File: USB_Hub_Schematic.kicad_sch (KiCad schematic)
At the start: 0 parts

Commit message: Started KiCAD
Put all relevant ports/chips into KiCAD
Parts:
- added Card1: TF PUSH, lcsc_easyeda:TF-SMD_TF-PUSH, symbol lcsc_easyeda:TFPUSH
- added U1: CH339W_C25503971, lcsc_easyeda:QFN-68_L8.0-W8.0-P0.40-BL-EP5.5, symbol lcsc_easyeda:CH339W_C25503971
- added USB1, USB2: TYPE-C 16PIN 2MD, lcsc_easyeda:USB-C-SMD_TYPE-C-16PIN-2MD-073, symbol lcsc_easyeda:TYPE-C16PIN2MD
- added USB3, USB4: 10.0 QHHTZB6.3, lcsc_easyeda:USB-A-TH_10.0QHHTZB6.3, symbol lcsc_easyeda:10.0QHHTZB6.3

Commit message: New parts
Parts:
- removed U1: CH339W_C25503971, lcsc_easyeda:QFN-68_L8.0-W8.0-P0.40-BL-EP5.5, symbol lcsc_easyeda:CH339W_C25503971
- removed USB1, USB2: TYPE-C 16PIN 2MD, lcsc_easyeda:USB-C-SMD_TYPE-C-16PIN-2MD-073, symbol lcsc_easyeda:TYPE-C16PIN2MD
- removed USB3, USB4: 10.0 QHHTZB6.3, lcsc_easyeda:USB-A-TH_10.0QHHTZB6.3, symbol lcsc_easyeda:10.0QHHTZB6.3
- added U1: Microchip, lcsc_easyeda:VQFN-100_L12.0-W12.0-P0.40-TL-EP8.0, symbol lcsc_easyeda:USB5807C_KD
- added U2: USB-C Male, lcsc_easyeda:USB-C-SMD_TYPE-C-24P-GTJB-040, symbol lcsc_easyeda:TYPE-C24P-GTJB040
- added U3: USB-A Male, lcsc_easyeda:USB-3.0-A-SMD_HC-USB3.0-C26, symbol lcsc_easyeda:HC-USB3.0-C26
- added U4, U5: Multiplexer, lcsc_easyeda:DHVQFN-20_L4.5-W2.5-P0.50-BL-EP, symbol lcsc_easyeda:HD3SS3212IRKSR
- added U6: SD Reader, lcsc_easyeda:HQFN-32_L5.0-W5.0-P0.50-BL-EP3.0, symbol lcsc_easyeda:GL3224-OIY04
- added USB1, USB2: USB-C Female, lcsc_easyeda:TYPE-C-SMD_C9900025773, symbol lcsc_easyeda:TYPE-C24PQT143
- added USB3, USB4: USB-A Female, lcsc_easyeda:USB-A-SMD_U-A-39SS-W-1, symbol lcsc_easyeda:U-A-39SS-W-1
- renumbered Card1 to microSD
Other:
- moved on the sheet: microSD

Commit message: KiCAD Work
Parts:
- removed U1: Microchip, lcsc_easyeda:VQFN-100_L12.0-W12.0-P0.40-TL-EP8.0, symbol lcsc_easyeda:USB5807C_KD
- added C1, C2, C3, C4, C6, C7, C8, C9: 0.1 uF, symbol Device:C
- added R1: 12k, symbol Device:R
- added R2: 900k, symbol Device:R
- added U1, U8: TUSB321, lcsc_easyeda:X2QFN-12_L1.6-W1.6-P0.40-BL, symbol lcsc_easyeda:TUSB321AIRWBR
- added U7: USB5926C-I/KD, lcsc_easyeda:VQFN-100_L12.0-W12.0-P0.40-TL-EP8.1, symbol lcsc_easyeda:USB5926C-I_KD
- added X1: 25MHz, lcsc_easyeda:OSC-SMD_4P-L3.2-W2.5-BL, symbol lcsc_easyeda:CO32H4-25.000-33JDTSN
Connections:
- net GNDREF: now reaches USB3.10 (GND)
- net GNDREF: now also USB1.15 (EP), USB1.16 (EP), USB1.17 (EP), USB1.18 (EP), USB1.A1 (GND), USB1.A12 (GND), USB1.B1 (GND), USB1.B12 (GND), USB3.11 (GND), USB3.4 (GND), USB3.7 (GND), USB4.10 (GND), USB4.11 (GND), USB4.4 (GND), USB4.7 (GND), R1.1, U1.10 (GND), U7.101 (EP), U7.23 (TESTEN)
- net at USB3.2 (D-): now also U7.87 (USB2DN_DM4/PRT_DIS_M4)
- net at USB3.3 (D+): now also U7.86 (USB2DN_DP4/PRT_DIS_P4)
- net at USB3.5 (SSRX-): now also U7.92 (USB3DN_RXDM4)
- net at USB3.6 (SSRX+): now also U7.91 (USB3DN_RXDP4)
- net at USB3.8 (SSTX-): now also C1.2
- net at USB3.9 (SSTX+): now also C2.2
- net at USB4.2 (D-): now also U7.44 (USB2DN_DM3/PRT_DIS_M3)
- net at USB4.3 (D+): now also U7.43 (USB2DN_DP3/PRT_DIS_P3)
- net at USB4.5 (SSRX-): now also U7.49 (USB3DN_RXDM3)
- net at USB4.6 (SSRX+): now also U7.48 (USB3DN_RXDP3)
- net at USB4.8 (SSTX-): now also C3.2
- net at USB4.9 (SSTX+): now also C4.2
- net at USB1.A10 (SSRXn2): now also U7.34 (USB3DN_RXDM2A)
- net at USB1.A11 (SSRXp2): now also U7.33 (USB3DN_RXDP2A)
- net at USB1.A2 (SSTXP1): now also C7.2
- net at USB1.A3 (SSTXn1): now also C6.2
- net at USB1.A4 (VBUS): now also USB1.A9 (VBUS)
- net at USB1.A5 (CC1): now also U1.1 (CC1)
- net at USB1.A6 (DP1): now also USB1.B6 (DP2), U7.35 (USB2DN_DP6/PRT_DIS_P6)
- net at USB1.A7 (DN1): now also USB1.B7 (DN2), U7.36 (USB2DN_DM6/PRT_DIS_M6)
- net at USB1.B10 (SSRXn1): now also U7.41 (USB3DN_RXDM2B)
- net at USB1.B11 (SSRXp1): now also U7.40 (USB3DN_RXDP2B)
- net at USB1.B2 (SSTXp2): now also C9.2
- net at USB1.B3 (SSTXn2): now also C8.2
- net at USB1.B4 (VBUS): now also USB1.B9 (VBUS)
- net at USB1.B5 (CC2): now also U1.2 (CC2)
- new net: R1.2, U7.1 (RBIAS)
- new net: U7.10 (VDD12), U7.17 (VDD12), U7.26 (VDD12), U7.32 (VDD12), U7.39 (VDD12), U7.47 (VDD12)
- new net: U7.2 (VDD33), U7.27 (VDD33), U7.42 (VDD33), U7.5 (VDD33)
- new net: C7.1, U7.30 (USB3DN_TXDP2A)
- new net: C6.1, U7.31 (USB3DN_TXDM2A)
- new net: C9.1, U7.37 (USB3DN_TXDP2B)
- new net: C8.1, U7.38 (USB3DN_TXDM2B)
- new net: C4.1, U7.45 (USB3DN_TXDP3)
- new net: C3.1, U7.46 (USB3DN_TXDM3)
- new net: U7.54 (VDD33), U7.64 (VDD33), U7.72 (VDD33), U7.93 (VDD33)
- new net: U7.59 (VDD12), U7.78 (VDD12), U7.83 (VDD12), U7.90 (VDD12), U7.98 (VDD12)
- new net: C2.1, U7.88 (USB3DN_TXDP4)
- new net: C1.1, U7.89 (USB3DN_TXDM4)
- new net: U1.12 (VDD), U1.4 (PORT)
- new net: R2.1, U1.5 (VBUS_DET)
- no-connect marks 0 -> 7
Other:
- note added: "1.2V PWR"
- note added: "3.3V PWR"
- note added: "CONNECT VBUS TO 5V POWER"
- moved on the sheet: microSD

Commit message: Continued schematics
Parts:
- removed U5: Multiplexer, lcsc_easyeda:DHVQFN-20_L4.5-W2.5-P0.50-BL-EP, symbol lcsc_easyeda:HD3SS3212IRKSR
- removed microSD: TF PUSH, lcsc_easyeda:TF-SMD_TF-PUSH, symbol lcsc_easyeda:TFPUSH
- added Card1: SD Reader, lcsc_easyeda:TF-SMD_TF-PUSH, symbol lcsc_easyeda:TFPUSH
- added D1: LED, symbol Device:LED
- added R3: 4.7k, symbol Device:R
- added R4: 680, 1%, symbol Device:R
- added R5: 330, symbol Device:R
- added X2: 25MHz, lcsc_easyeda:OSC-SMD_4P-L3.2-W2.5-BL, symbol lcsc_easyeda:CO32H4-25.000-33JDTSN
- C2: value 0.1 uF -> 1uF
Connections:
- net GNDREF: now also C2.1, C2.2, U6.24 (VUHSI), U6.27 (GND), U6.28 (SD_WP), U6.33 (EP), R4.2
- net at U7.6 (USB2DN_DP1/PRT_DIS_P1): now also USB3.3 (D+)
- net at U7.7 (USB2DN_DM1/PRT_DIS_M1): now also USB3.2 (D-)
- net at U7.86 (USB2DN_DP4/PRT_DIS_P4): now also U6.32 (DP); no longer USB3.3 (D+)
- net at U7.87 (USB2DN_DM4/PRT_DIS_M4): now also U6.31 (DM); no longer USB3.2 (D-)
- net at U7.88 (USB3DN_TXDP4): now also U6.2 (TXP); no longer C2.1
- net at U7.89 (USB3DN_TXDM4): now also U6.1 (TXN); no longer C1.1
- net at U7.91 (USB3DN_RXDP4): now also U6.5 (RXP); no longer USB3.6 (SSRX+)
- net at U7.92 (USB3DN_RXDM4): now also U6.4 (RXN); no longer USB3.5 (SSRX-)
- net at U1.12 (VDD): now also R2.2, R3.1; no longer U1.4 (PORT)
- net at USB3.8 (SSTX-): no longer C1.2
- net at USB3.9 (SSTX+): no longer C2.2
- net at U6.14 (LED): now also D1.1 (K)
- net at U6.18 (SD_D1): now also Card1.8 (DAT1)
- net at U6.19 (SD_D0): now also Card1.7 (DAT0)
- net at U6.20 (SD_CK): now also Card1.5 (CLX)
- net at U6.21 (SD_CM): now also Card1.3 (CMD)
- net at U6.22 (SD_D3): now also Card1.2 (CD/DAT3)
- net at U6.23 (SD_D2): now also Card1.1 (DAT2)
- net at U6.26 (SD_VCC): now also C1.2, Card1.4 (VDD)
- net at U6.29 (SD_CDZ): now also Card1.CD
- net at U6.9 (RTERM): now also R4.1
- net at USB1.A4 (VBUS), USB1.A9 (VBUS): now also USB1.B4 (VBUS), USB1.B9 (VBUS)
- new net: R3.2, U1.4 (PORT)
- new net: D1.2 (A), R5.2
- new net: C1.1, Card1.10, Card1.11, Card1.12, Card1.13, Card1.6 (VSS)
- no-connect marks 7 -> 18
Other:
- note added: "TO 3.3V PWR"
- note added: "VBUS TO 5V POWER"

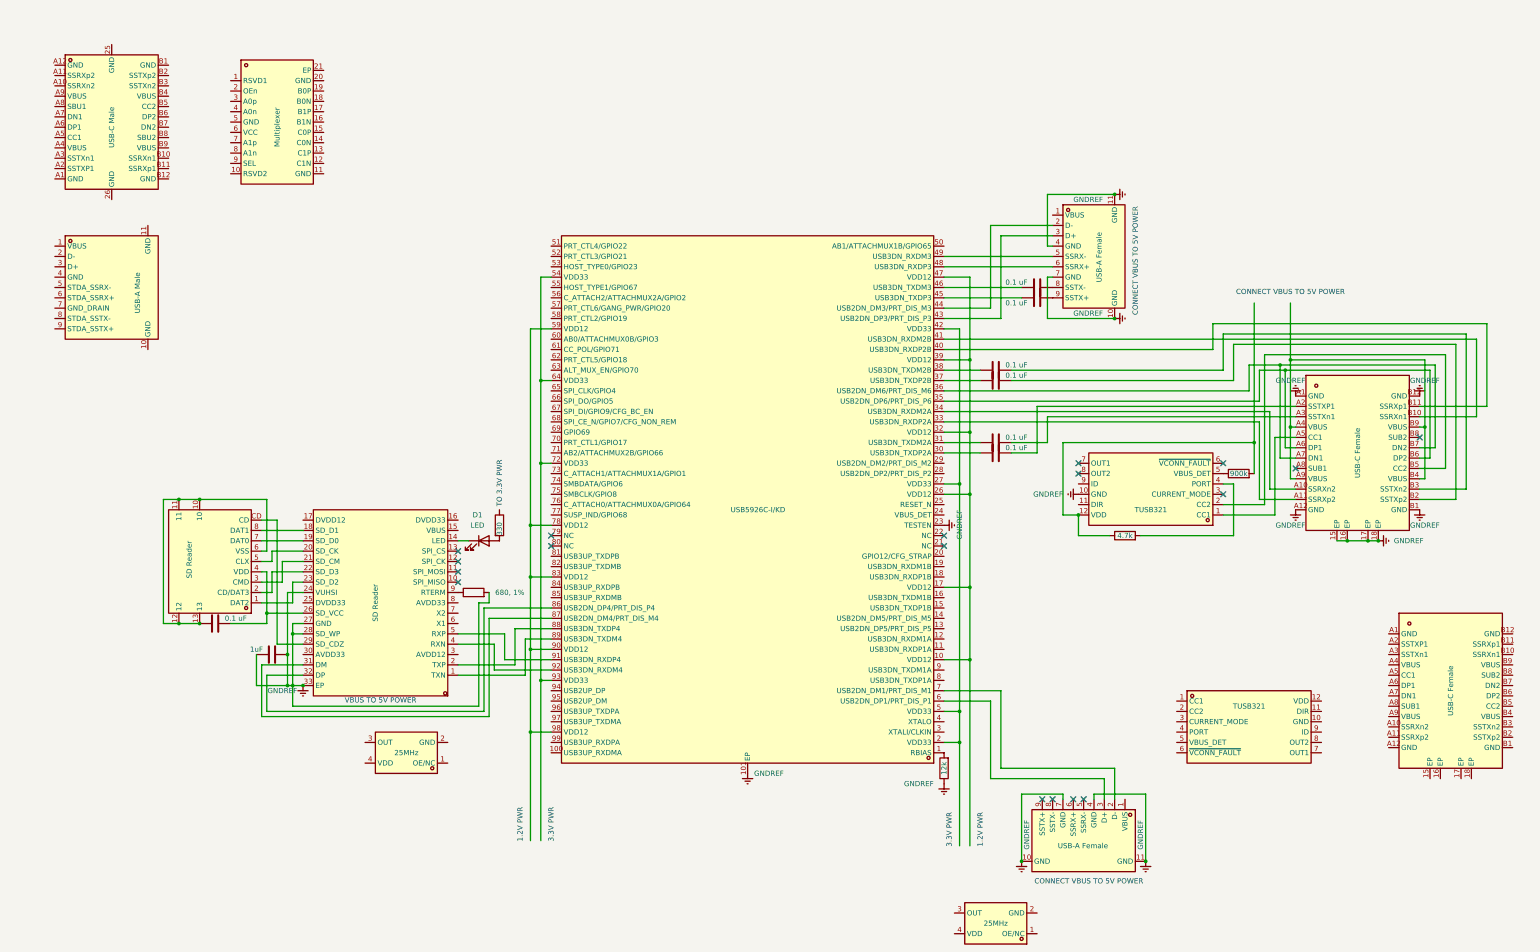
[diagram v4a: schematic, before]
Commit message: New schematic
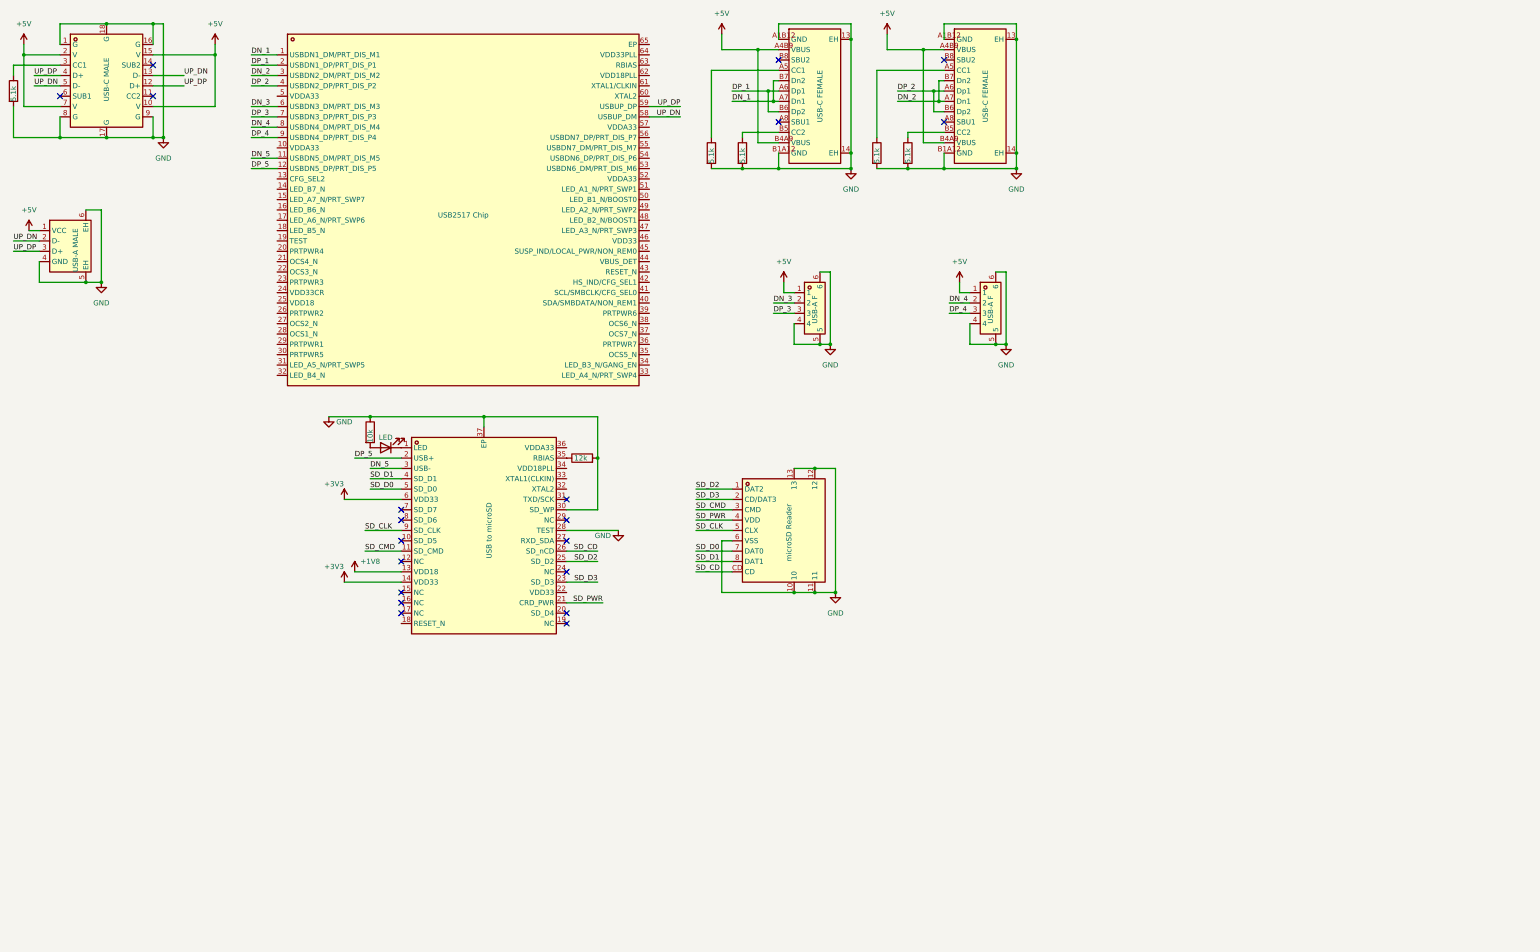
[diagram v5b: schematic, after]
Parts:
- removed C1, C3, C4, C6, C7, C8, C9: 0.1 uF, symbol Device:C
- removed C2: 1uF, symbol Device:C
- removed U1, U8: TUSB321, lcsc_easyeda:X2QFN-12_L1.6-W1.6-P0.40-BL, symbol lcsc_easyeda:TUSB321AIRWBR
- removed U2: USB-C Male, lcsc_easyeda:USB-C-SMD_TYPE-C-24P-GTJB-040, symbol lcsc_easyeda:TYPE-C24P-GTJB040
- removed U3: USB-A Male, lcsc_easyeda:USB-3.0-A-SMD_HC-USB3.0-C26, symbol lcsc_easyeda:HC-USB3.0-C26
- removed U4: Multiplexer, lcsc_easyeda:DHVQFN-20_L4.5-W2.5-P0.50-BL-EP, symbol lcsc_easyeda:HD3SS3212IRKSR
- removed U6: SD Reader, lcsc_easyeda:HQFN-32_L5.0-W5.0-P0.50-BL-EP3.0, symbol lcsc_easyeda:GL3224-OIY04
- removed U7: USB5926C-I/KD, lcsc_easyeda:VQFN-100_L12.0-W12.0-P0.40-TL-EP8.1, symbol lcsc_easyeda:USB5926C-I_KD
- removed USB1, USB2: USB-C Female, lcsc_easyeda:TYPE-C-SMD_C9900025773, symbol lcsc_easyeda:TYPE-C24PQT143
- removed USB3, USB4: USB-A Female, lcsc_easyeda:USB-A-SMD_U-A-39SS-W-1, symbol lcsc_easyeda:U-A-39SS-W-1
- removed X1, X2: 25MHz, lcsc_easyeda:OSC-SMD_4P-L3.2-W2.5-BL, symbol lcsc_easyeda:CO32H4-25.000-33JDTSN
- added R6: 10k, symbol Device:R
- added R7: 12k, symbol Device:R
- added U1: USB2517 Chip, lcsc_easyeda:QFN-64_L9.0-W9.0-P0.50-BL-EP4.8, symbol lcsc_easyeda:USB2517-JZX
- added U2: USB to microSD, lcsc_easyeda:QFN-36_L6.0-W6.0-P0.50-EP4.2, symbol lcsc_easyeda:USB2244I-AEZG-06-TR
- added U4, U6: USB-A F, lcsc_easyeda:USB-A-TH_USB1125-GF-B, symbol lcsc_easyeda:USB1125-GF-B
- added USB1, USB2: USB-C FEMALE, lcsc_easyeda:USB-C-SMD_TYPE-C-16PIN-2MD-073, symbol lcsc_easyeda:TYPE-C16PIN2MD
- added USB3: USB-A MALE, lcsc_easyeda:USB-A-TH_XBDM-9101-018, symbol lcsc_easyeda:XBDM-9101-018
- added USB4: USB-C MALE, lcsc_easyeda:USB-C-SMD_918-118A2021Y40006, symbol lcsc_easyeda:918-118A2021Y40006
- Card1: value SD Reader -> microSD Reader
- R1: value 12k -> 5.1k; footprint (none) -> Resistor_SMD:R_01005_0402Metric
- R2: value 900k -> 5.1k; footprint (none) -> Resistor_SMD:R_01005_0402Metric
- R3: value 4.7k -> 5.1k; footprint (none) -> Resistor_SMD:R_01005_0402Metric
- R4: value 680, 1% -> 5.1k; footprint (none) -> Resistor_SMD:R_01005_0402Metric
- R5: value 330 -> 5.1k; footprint (none) -> Resistor_SMD:R_01005_0402Metric
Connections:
- net GND: now reaches R1.2
- net GND: now also Card1.10, Card1.11, Card1.12, Card1.13, Card1.6 (VSS), R2.2, R3.2, R4.2, R5.2, R6.1, R7.2, U2.28 (TEST), U2.30 (SD_WP), U2.37 (EP), U4.4, U4.5, U4.6, U6.4, U6.5, U6.6, USB1.13 (EH), USB1.14 (EH), USB1.A1B12 (GND), USB1.B1A12 (GND), USB2.13 (EH), USB2.14 (EH), USB2.A1B12 (GND), USB2.B1A12 (GND), USB3.4 (GND), USB3.5 (EH), USB3.6 (EH), USB4.1 (G), USB4.16 (G), USB4.17 (G), USB4.18 (G), USB4.8 (G), USB4.9 (G)
- net at R3.1: now also USB2.A5 (CC1); no longer R2.2
- net at R2.1: now also USB1.A5 (CC1)
- net at D1.1 (K): now also U2.1 (LED)
- net at D1.2 (A): now also R6.2; no longer R5.2
- net at R5.1: now also USB4.3 (CC1)
- net SD_D2: now reaches Card1.1 (DAT2)
- net SD_D2: now also U2.25 (SD_D2)
- net SD_D3: now reaches Card1.2 (CD/DAT3)
- net SD_D3: now also U2.23 (SD_D3)
- net SD_CMD: now reaches Card1.3 (CMD)
- net SD_CMD: now also U2.11 (SD_CMD)
- net SD_PWR: now reaches Card1.4 (VDD)
- net SD_PWR: now also U2.21 (CRD_PWR)
- net SD_CLK: now reaches Card1.5 (CLX)
- net SD_CLK: now also U2.9 (SD_CLK)
- net SD_D0: now reaches Card1.7 (DAT0)
- net SD_D0: now also U2.5 (SD_D0)
- net SD_D1: now reaches Card1.8 (DAT1)
- net SD_D1: now also U2.4 (SD_D1)
- net SD_CD: now reaches Card1.CD
- net SD_CD: now also U2.26 (SD_nCD)
- net at R4.1: now also USB2.B5 (CC2)
- net GNDREF: no longer names the net of R1.1
- net GNDREF: now also USB1.B5 (CC2); no longer R4.2
- new net: R7.1, U2.35 (RBIAS)
- new net +1V8: U2.13 (VDD18)
- new net +3V3: U2.14 (VDD33), U2.6 (VDD33)
- new net +5V: U4.1, U6.1, USB1.A4B9 (VBUS), USB1.B4A9 (VBUS), USB2.A4B9 (VBUS), USB2.B4A9 (VBUS), USB3.1 (VCC), USB4.10 (V), USB4.15 (V), USB4.2 (V), USB4.7 (V)
- new net DN_1: U1.1 (USBDN1_DM/PRT_DIS_M1), USB1.A7 (Dn1), USB1.B7 (Dn2)
- new net DN_2: U1.3 (USBDN2_DM/PRT_DIS_M2), USB2.A7 (Dn1), USB2.B7 (Dn2)
- new net DN_3: U1.6 (USBDN3_DM/PRT_DIS_M3), U4.2
- new net DN_4: U1.8 (USBDN4_DM/PRT_DIS_M4), U6.2
- new net DN_5: U1.11 (USBDN5_DM/PRT_DIS_M5), U2.3 (USB-)
- new net DP_1: U1.2 (USBDN1_DP/PRT_DIS_P1), USB1.A6 (Dp1), USB1.B6 (Dp2)
- new net DP_2: U1.4 (USBDN2_DP/PRT_DIS_P2), USB2.A6 (Dp1), USB2.B6 (Dp2)
- new net DP_3: U1.7 (USBDN3_DP/PRT_DIS_P3), U4.3
- new net DP_4: U1.9 (USBDN4_DP/PRT_DIS_P4), U6.3
- new net DP_5: U1.12 (USBDN5_DP/PRT_DIS_P5), U2.2 (USB+)
- new net UP_DN: U1.58 (USBUP_DM), USB3.2 (D-), USB4.13 (D-), USB4.5 (D-)
- new net UP_DP: U1.59 (USBUP_DP), USB3.3 (D+), USB4.12 (D+), USB4.4 (D+)
- no-connect marks 18 -> 20
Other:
- note removed: "1.2V PWR"
- note removed: "3.3V PWR"
- note removed: "CONNECT VBUS TO 5V POWER"
- note removed: "TO 3.3V PWR"
- note removed: "VBUS TO 5V POWER"
